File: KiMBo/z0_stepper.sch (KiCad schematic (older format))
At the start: 25 parts, among them U23 TMC2130

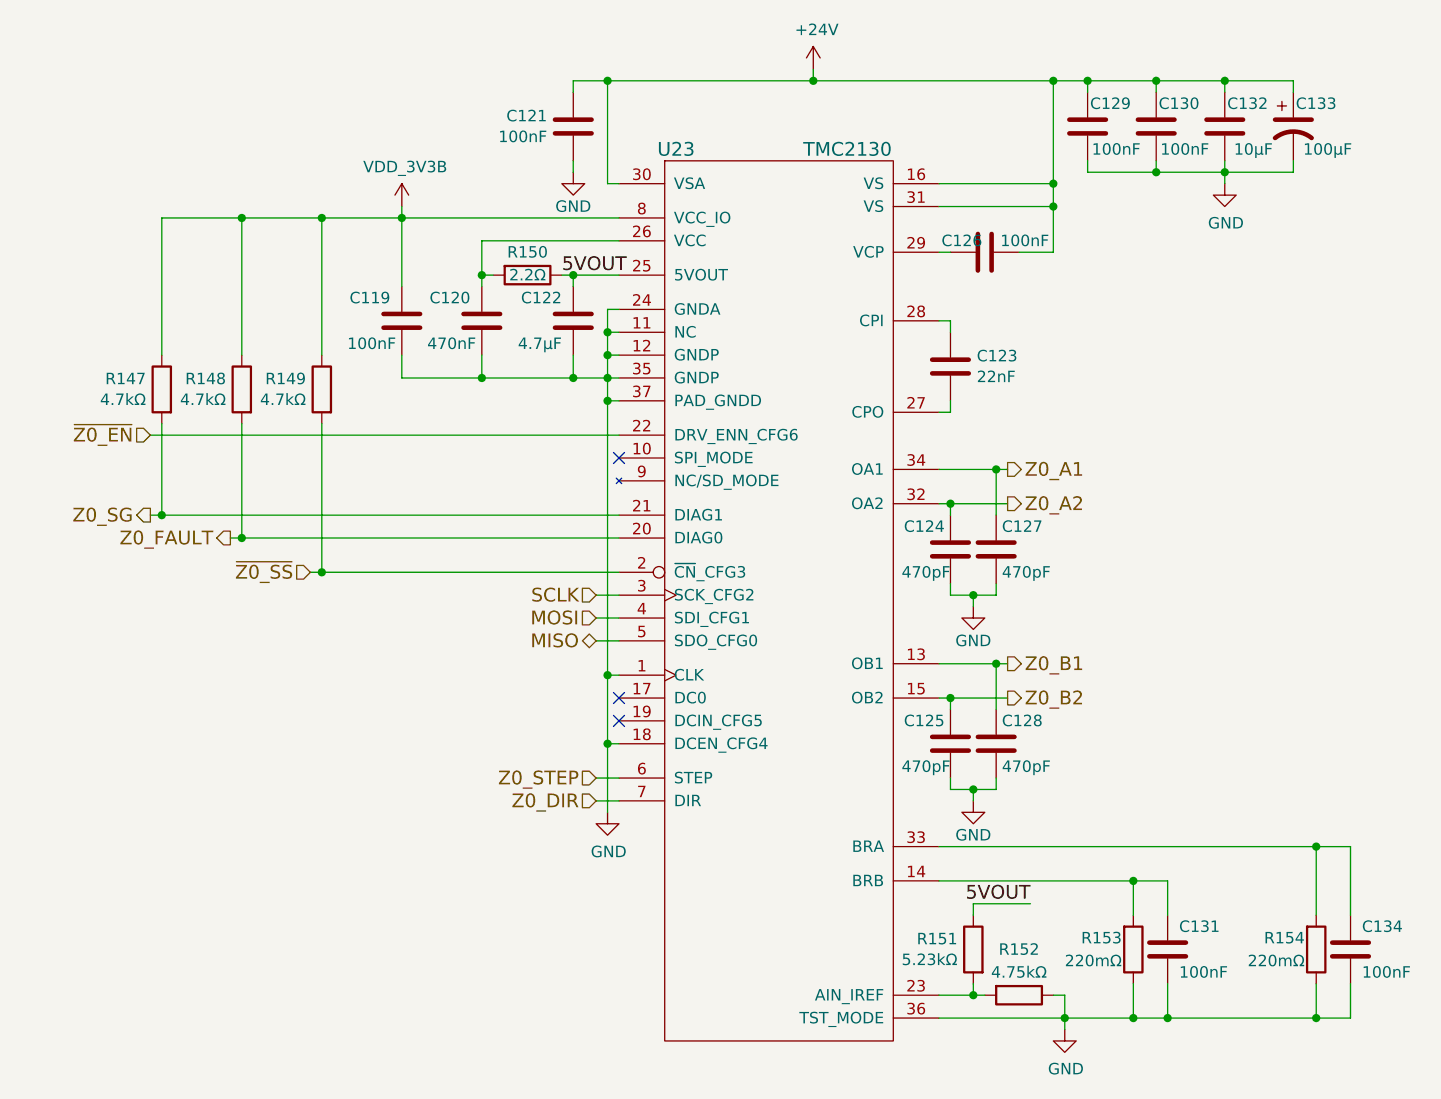
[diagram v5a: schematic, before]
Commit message: Connect X and Z stepper driver open-drain DIAG0 and DIAG1 lines together
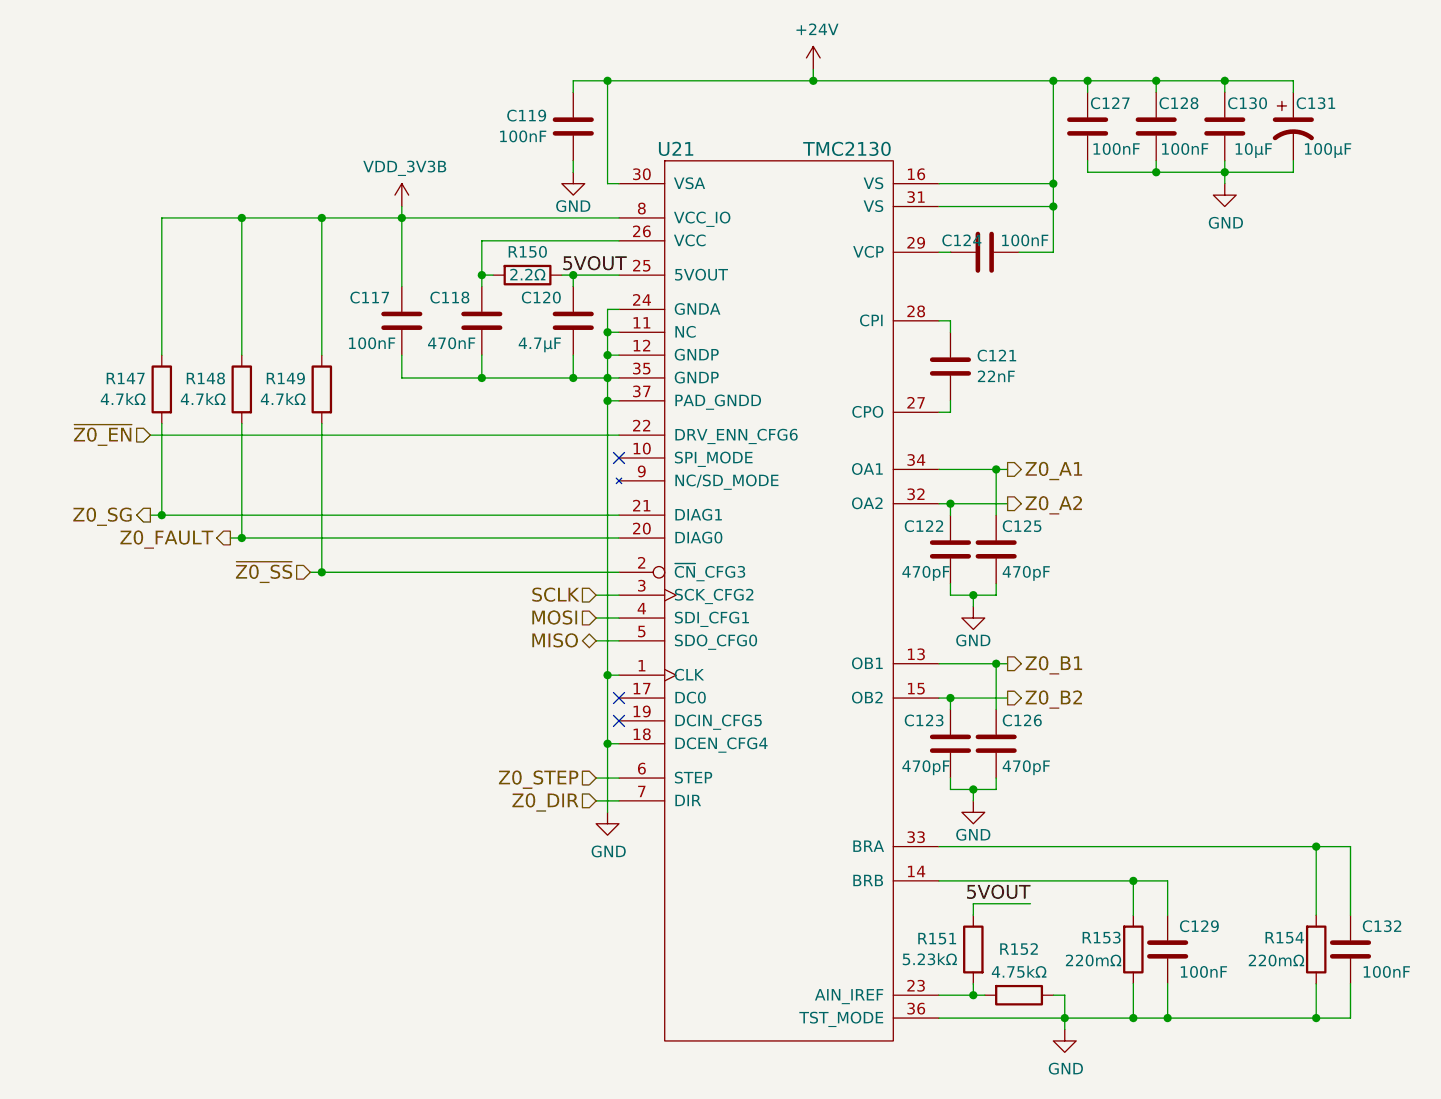
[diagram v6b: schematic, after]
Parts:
- renumbered C119 to C117, C120 to C118, C121 to C119, C122 to C120, C123 to C121, C124 to C122, C125 to C123, C126 to C124, C127 to C125, C128 to C126, C129 to C127, C130 to C128, C131 to C129, C132 to C130, C133 to C131, C134 to C132, U23 to U21
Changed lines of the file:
@@
 Z0_SG
 $Comp
-L C C121
+L C C119
 U 1 1 58C0C3C9
 P 7100 3150
-F 0 "C121" H 6986 3104 50  0000 R CNN
+F 0 "C119" H 6986 3104 50  0000 R CNN
 F 1 "100nF" H 6986 3195 50  0000 R CNN
 F 2 "Capacitors_SMD:C_0603" H 7138 3000 50  0001 C CNN
@@
 $EndComp
 $Comp
-L C C126
+L C C124
 U 1 1 58C0C3D0
 P 8900 3700
-F 0 "C126" V 8850 3600 50  0000 C CNN
+F 0 "C124" V 8850 3600 50  0000 C CNN
 F 1 "100nF" V 8850 3875 50  0000 C CNN
 F 2 "Capacitors_SMD:C_0603" H 8938 3550 50  0001 C CNN
@@
 $EndComp
 $Comp
-L CP1 C133
+L CP1 C131
 U 1 1 58C0C3D7
 P 10250 3150
-F 0 "C133" H 10350 3250 50  0000 C CNN
+F 0 "C131" H 10350 3250 50  0000 C CNN
 F 1 "100μF" H 10400 3050 50  0000 C CNN
 F 2 "Capacitors_SMD:c_elec_8x10" H 10250 3150 50  0001 C CNN
@@
 $EndComp
 $Comp
-L C C129
+L C C127
 U 1 1 58C0C3DE
 P 9350 3150
-F 0 "C129" H 9250 3250 50  0000 C CNN
+F 0 "C127" H 9250 3250 50  0000 C CNN
 F 1 "100nF" H 9225 3050 50  0000 C CNN
 F 2 "Capacitors_SMD:C_0603" H 9388 3000 50  0001 C CNN
@@
 $EndComp
 $Comp
-L GND #PWR0226
+L GND #PWR0216
 U 1 1 58C0C3E5
 P 7100 3350
-F 0 "#PWR0226" H 7100 3100 50  0001 C CNN
+F 0 "#PWR0216" H 7100 3100 50  0001 C CNN
 F 1 "GND" H 7100 3200 50  0000 C CNN
 F 2 "" H 7100 3350 50  0000 C CNN
@@
 $EndComp
 $Comp
-L C C130
+L C C128
 U 1 1 58C0C3EB
 P 9650 3150
-F 0 "C130" H 9550 3250 50  0000 C CNN
+F 0 "C128" H 9550 3250 50  0000 C CNN
 F 1 "100nF" H 9525 3050 50  0000 C CNN
 F 2 "Capacitors_SMD:C_0603" H 9688 3000 50  0001 C CNN
@@
 $EndComp
 $Comp
-L GND #PWR0227
+L GND #PWR0217
 U 1 1 58C0C3F2
 P 9950 3400
-F 0 "#PWR0227" H 9950 3150 50  0001 C CNN
+F 0 "#PWR0217" H 9950 3150 50  0001 C CNN
 F 1 "GND" H 9955 3227 50  0000 C CNN
 F 2 "" H 9950 3400 50  0000 C CNN
@@
 $EndComp
 $Comp
-L +24V #PWR0228
+L +24V #PWR0218
 U 1 1 58C0C3F8
 P 8150 2900
-F 0 "#PWR0228" H 8150 2750 50  0001 C CNN
+F 0 "#PWR0218" H 8150 2750 50  0001 C CNN
 F 1 "+24V" H 8165 3073 50  0000 C CNN
 F 2 "" H 8150 2900 50  0000 C CNN
@@
 $EndComp
 $Comp
-L C C123
+L C C121
 U 1 1 58C0C3FE
 P 8750 4200
-F 0 "C123" H 8865 4246 50  0000 L CNN
+F 0 "C121" H 8865 4246 50  0000 L CNN
 F 1 "22nF" H 8865 4155 50  0000 L CNN
 F 2 "Capacitors_SMD:C_0402" H 8788 4050 50  0001 C CNN
@@
 $EndComp
 $Comp
-L GND #PWR0229
+L GND #PWR0219
 U 1 1 58C0C413
 P 9250 7100
-F 0 "#PWR0229" H 9250 6850 50  0001 C CNN
+F 0 "#PWR0219" H 9250 6850 50  0001 C CNN
 F 1 "GND" H 9255 6927 50  0000 C CNN
 F 2 "" H 9250 7100 50  0000 C CNN
@@
 $EndComp
 $Comp
-L C C120
+L C C118
 U 1 1 58C0C421
 P 6700 4000
-F 0 "C120" H 6750 4100 50  0000 L CNN
+F 0 "C118" H 6750 4100 50  0000 L CNN
 F 1 "470nF" H 6725 3900 50  0000 L CNN
 F 2 "Capacitors_SMD:C_0603" H 6738 3850 50  0001 C CNN
@@
 NoConn ~ 7300 5750
 $Comp
-L GND #PWR0230
+L GND #PWR0220
 U 1 1 58C0C436
 P 7250 6150
-F 0 "#PWR0230" H 7250 5900 50  0001 C CNN
+F 0 "#PWR0220" H 7250 5900 50  0001 C CNN
 F 1 "GND" H 7255 5977 50  0000 C CNN
 F 2 "" H 7250 6150 50  0000 C CNN
@@
 $EndComp
 $Comp
-L C C131
+L C C129
 U 1 1 58C0C43C
 P 9700 6750
-F 0 "C131" H 9750 6850 50  0000 L CNN
+F 0 "C129" H 9750 6850 50  0000 L CNN
 F 1 "100nF" H 9750 6650 50  0000 L CNN
 F 2 "Capacitors_SMD:C_0603" H 9738 6600 50  0001 C CNN
@@
 NoConn ~ 7300 4600
 $Comp
-L C C122
+L C C120
 U 1 1 58C0C44E
 P 7100 4000
-F 0 "C122" H 7150 4100 50  0000 L CNN
+F 0 "C120" H 7150 4100 50  0000 L CNN
 F 1 "4.7μF" H 7150 3900 50  0000 L CNN
 F 2 "Capacitors_SMD:C_0402" H 7138 3850 50  0001 C CNN
@@
 $EndComp
 $Comp
-L C C134
+L C C132
 U 1 1 58C0C46C
 P 10500 6750
-F 0 "C134" H 10550 6850 50  0000 L CNN
+F 0 "C132" H 10550 6850 50  0000 L CNN
 F 1 "100nF" H 10550 6650 50  0000 L CNN
 F 2 "Capacitors_SMD:C_0603" H 10538 6600 50  0001 C CNN
@@
 $EndComp
 $Comp
-L C C124
+L C C122
 U 1 1 58C0C473
 P 8750 5000
-F 0 "C124" H 8775 5100 50  0000 L CNN
+F 0 "C122" H 8775 5100 50  0000 L CNN
 F 1 "470pF" H 8750 4900 50  0000 L CNN
 F 2 "Capacitors_SMD:C_0603" H 8788 4850 50  0001 C CNN
@@
 $EndComp
 $Comp
-L GND #PWR0231
+L GND #PWR0221
 U 1 1 58C0C47A
 P 8850 5250
-F 0 "#PWR0231" H 8850 5000 50  0001 C CNN
+F 0 "#PWR0221" H 8850 5000 50  0001 C CNN
 F 1 "GND" H 8850 5100 50  0000 C CNN
 F 2 "" H 8850 5250 50  0000 C CNN
@@
 $EndComp
 $Comp
-L C C127
+L C C125
 U 1 1 58C0C480
 P 8950 5000
-F 0 "C127" H 8975 5100 50  0000 L CNN
+F 0 "C125" H 8975 5100 50  0000 L CNN
 F 1 "470pF" H 8975 4900 50  0000 L CNN
 F 2 "Capacitors_SMD:C_0603" H 8988 4850 50  0001 C CNN
@@
 $EndComp
 $Comp
-L C C125
+L C C123
 U 1 1 58C0C487
 P 8750 5850
-F 0 "C125" H 8775 5950 50  0000 L CNN
+F 0 "C123" H 8775 5950 50  0000 L CNN
 F 1 "470pF" H 8750 5750 50  0000 L CNN
 F 2 "Capacitors_SMD:C_0603" H 8788 5700 50  0001 C CNN
@@
 $EndComp
 $Comp
-L GND #PWR0232
+L GND #PWR0222
 U 1 1 58C0C48E
 P 8850 6100
-F 0 "#PWR0232" H 8850 5850 50  0001 C CNN
+F 0 "#PWR0222" H 8850 5850 50  0001 C CNN
 F 1 "GND" H 8850 5950 50  0000 C CNN
 F 2 "" H 8850 6100 50  0000 C CNN
@@
 $EndComp
 $Comp
-L C C128
+L C C126
 U 1 1 58C0C494
 P 8950 5850
-F 0 "C128" H 8975 5950 50  0000 L CNN
+F 0 "C126" H 8975 5950 50  0000 L CNN
 F 1 "470pF" H 8975 5750 50  0000 L CNN
 F 2 "Capacitors_SMD:C_0603" H 8988 5700 50  0001 C CNN
@@
 $EndComp
 $Comp
-L TMC2130 U23
+L TMC2130 U21
 U 1 1 58C0C49B
 P 8000 4750
-F 0 "U23" H 7550 6250 60  0000 C CNN
+F 0 "U21" H 7550 6250 60  0000 C CNN
 F 1 "TMC2130" H 8300 6250 60  0000 C CNN
 F 2 "" H 8000 5050 60  0001 C CNN
@@
 Connection ~ 5650 3550
 $Comp
-L C C132
+L C C130
 U 1 1 58C0C51A
 P 9950 3150
-F 0 "C132" H 9850 3250 50  0000 C CNN
+F 0 "C130" H 9850 3250 50  0000 C CNN
 F 1 "10μF" H 9825 3050 50  0000 C CNN
 F 2 "Capacitors_SMD:C_0805" H 9988 3000 50  0001 C CNN
@@
 	5300 3550 7300 3550
 $Comp
-L VDD_3V3B #PWR0233
+L VDD_3V3B #PWR0223
 U 1 1 5A313878
 P 6350 3500
-F 0 "#PWR0233" H 6350 3350 50  0001 C CNN
+F 0 "#PWR0223" H 6350 3350 50  0001 C CNN
 F 1 "VDD_3V3B" H 6365 3673 50  0000 C CNN
 F 2 "" H 6350 3500 50  0000 C CNN
@@
 $EndComp
 $Comp
-L C C119
+L C C117
 U 1 1 5A89B9DA
 P 6350 4000
-F 0 "C119" H 6400 4100 50  0000 L CNN
+F 0 "C117" H 6400 4100 50  0000 L CNN
 F 1 "100nF" H 6375 3900 50  0000 L CNN
 F 2 "Capacitors_SMD:C_0603" H 6388 3850 50  0001 C CNN

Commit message: Leave SPI0 free for a display, reassign pins so SPI1 is available
Fix some typos/errors
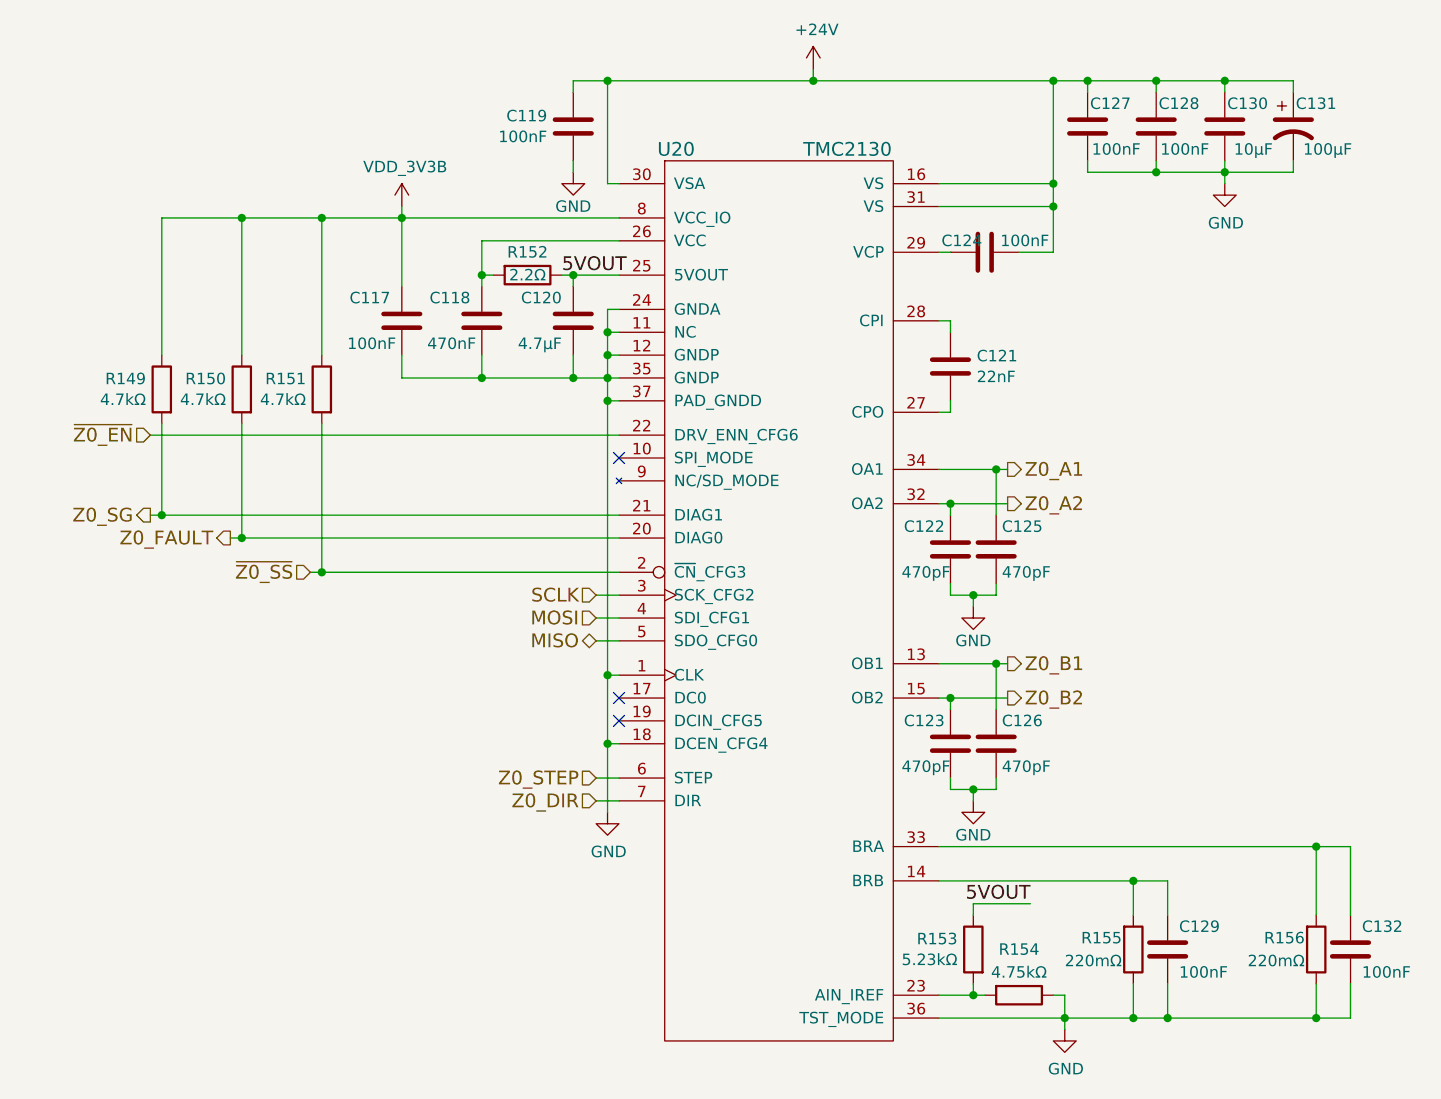
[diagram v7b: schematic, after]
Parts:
- renumbered R147 to R149, R148 to R150, R149 to R151, R150 to R152, R151 to R153, R152 to R154, R153 to R155, R154 to R156, U21 to U20
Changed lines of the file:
@@
 $EndComp
 $Comp
-L GND #PWR0216
+L GND #PWR0215
 U 1 1 58C0C3E5
 P 7100 3350
-F 0 "#PWR0216" H 7100 3100 50  0001 C CNN
+F 0 "#PWR0215" H 7100 3100 50  0001 C CNN
 F 1 "GND" H 7100 3200 50  0000 C CNN
 F 2 "" H 7100 3350 50  0000 C CNN
@@
 $EndComp
 $Comp
-L GND #PWR0217
+L GND #PWR0216
 U 1 1 58C0C3F2
 P 9950 3400
-F 0 "#PWR0217" H 9950 3150 50  0001 C CNN
+F 0 "#PWR0216" H 9950 3150 50  0001 C CNN
 F 1 "GND" H 9955 3227 50  0000 C CNN
 F 2 "" H 9950 3400 50  0000 C CNN
@@
 $EndComp
 $Comp
-L +24V #PWR0218
+L +24V #PWR0217
 U 1 1 58C0C3F8
 P 8150 2900
-F 0 "#PWR0218" H 8150 2750 50  0001 C CNN
+F 0 "#PWR0217" H 8150 2750 50  0001 C CNN
 F 1 "+24V" H 8165 3073 50  0000 C CNN
 F 2 "" H 8150 2900 50  0000 C CNN
@@
 $EndComp
 $Comp
-L R R154
+L R R156
 U 1 1 58C0C405
 P 10350 6750
-F 0 "R154" H 10300 6700 50  0000 R CNN
+F 0 "R156" H 10300 6700 50  0000 R CNN
 F 1 "220mΩ" H 10300 6800 50  0000 R CNN
 F 2 "" V 10280 6750 50  0001 C CNN
@@
 $EndComp
 $Comp
-L R R153
+L R R155
 U 1 1 58C0C40C
 P 9550 6750
-F 0 "R153" H 9500 6700 50  0000 R CNN
+F 0 "R155" H 9500 6700 50  0000 R CNN
 F 1 "220mΩ" H 9500 6800 50  0000 R CNN
 F 2 "" V 9480 6750 50  0001 C CNN
@@
 $EndComp
 $Comp
-L GND #PWR0219
+L GND #PWR0218
 U 1 1 58C0C413
 P 9250 7100
-F 0 "#PWR0219" H 9250 6850 50  0001 C CNN
+F 0 "#PWR0218" H 9250 6850 50  0001 C CNN
 F 1 "GND" H 9255 6927 50  0000 C CNN
 F 2 "" H 9250 7100 50  0000 C CNN
@@
 NoConn ~ 7300 5650
 $Comp
-L R R150
+L R R152
 U 1 1 58C0C41A
 P 6900 3800
-F 0 "R150" V 6800 3800 50  0000 C CNN
+F 0 "R152" V 6800 3800 50  0000 C CNN
 F 1 "2.2Ω" V 6900 3800 50  0000 C CNN
 F 2 "" V 6830 3800 50  0001 C CNN
@@
 NoConn ~ 7300 5750
 $Comp
-L GND #PWR0220
+L GND #PWR0219
 U 1 1 58C0C436
 P 7250 6150
-F 0 "#PWR0220" H 7250 5900 50  0001 C CNN
+F 0 "#PWR0219" H 7250 5900 50  0001 C CNN
 F 1 "GND" H 7255 5977 50  0000 C CNN
 F 2 "" H 7250 6150 50  0000 C CNN
@@
 Z0_FAULT
 $Comp
-L R R148
+L R R150
 U 1 1 58C0C444
 P 5650 4300
-F 0 "R148" H 5719 4346 50  0000 L CNN
+F 0 "R150" H 5719 4346 50  0000 L CNN
 F 1 "4.7kΩ" H 5719 4255 50  0000 L CNN
 F 2 "" V 5580 4300 50  0001 C CNN
@@
 5VOUT
 $Comp
-L R R151
+L R R153
 U 1 1 58C0C456
 P 8850 6750
-F 0 "R151" H 8919 6796 50  0000 L CNN
+F 0 "R153" H 8919 6796 50  0000 L CNN
 F 1 "5.23kΩ" H 8919 6705 50  0000 L CNN
 F 2 "" V 8780 6750 50  0001 C CNN
@@
 5VOUT
 $Comp
-L R R152
+L R R154
 U 1 1 58C0C45E
 P 9050 6950
-F 0 "R152" V 8850 6950 50  0000 C CNN
+F 0 "R154" V 8850 6950 50  0000 C CNN
 F 1 "4.75kΩ" V 8950 6950 50  0000 C CNN
 F 2 "" V 8980 6950 50  0001 C CNN
@@
 $EndComp
 $Comp
-L R R149
+L R R151
 U 1 1 58C0C465
 P 6000 4300
-F 0 "R149" H 6069 4346 50  0000 L CNN
+F 0 "R151" H 6069 4346 50  0000 L CNN
 F 1 "4.7kΩ" H 6069 4255 50  0000 L CNN
 F 2 "" V 5930 4300 50  0001 C CNN
@@
 $EndComp
 $Comp
-L GND #PWR0221
+L GND #PWR0220
 U 1 1 58C0C47A
 P 8850 5250
-F 0 "#PWR0221" H 8850 5000 50  0001 C CNN
+F 0 "#PWR0220" H 8850 5000 50  0001 C CNN
 F 1 "GND" H 8850 5100 50  0000 C CNN
 F 2 "" H 8850 5250 50  0000 C CNN
@@
 $EndComp
 $Comp
-L GND #PWR0222
+L GND #PWR0221
 U 1 1 58C0C48E
 P 8850 6100
-F 0 "#PWR0222" H 8850 5850 50  0001 C CNN
+F 0 "#PWR0221" H 8850 5850 50  0001 C CNN
 F 1 "GND" H 8850 5950 50  0000 C CNN
 F 2 "" H 8850 6100 50  0000 C CNN
@@
 $EndComp
 $Comp
-L TMC2130 U21
+L TMC2130 U20
 U 1 1 58C0C49B
 P 8000 4750
-F 0 "U21" H 7550 6250 60  0000 C CNN
+F 0 "U20" H 7550 6250 60  0000 C CNN
 F 1 "TMC2130" H 8300 6250 60  0000 C CNN
 F 2 "" H 8000 5050 60  0001 C CNN
@@
 	8750 6050 8750 6000
 $Comp
-L R R147
+L R R149
 U 1 1 58C0C50F
 P 5300 4300
-F 0 "R147" H 5369 4346 50  0000 L CNN
+F 0 "R149" H 5369 4346 50  0000 L CNN
 F 1 "4.7kΩ" H 5369 4255 50  0000 L CNN
 F 2 "" V 5230 4300 50  0001 C CNN
@@
 	5300 3550 7300 3550
 $Comp
-L VDD_3V3B #PWR0223
+L VDD_3V3B #PWR0222
 U 1 1 5A313878
 P 6350 3500
-F 0 "#PWR0223" H 6350 3350 50  0001 C CNN
+F 0 "#PWR0222" H 6350 3350 50  0001 C CNN
 F 1 "VDD_3V3B" H 6365 3673 50  0000 C CNN
 F 2 "" H 6350 3500 50  0000 C CNN
